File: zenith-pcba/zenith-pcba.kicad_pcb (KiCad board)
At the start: 2 copper layers, 45 parts, among them SW1 G4R152312, U1 XC7K70T-FBG676, U2 K4B4G1646E-BCNB, U3 CH347T, U4 AP63203WU, U5 TXS0101DB, U6 TXS0101DB, U7 TXS0101DB, U8 TXS0101DB, X1 SX5B8.000F1520F30

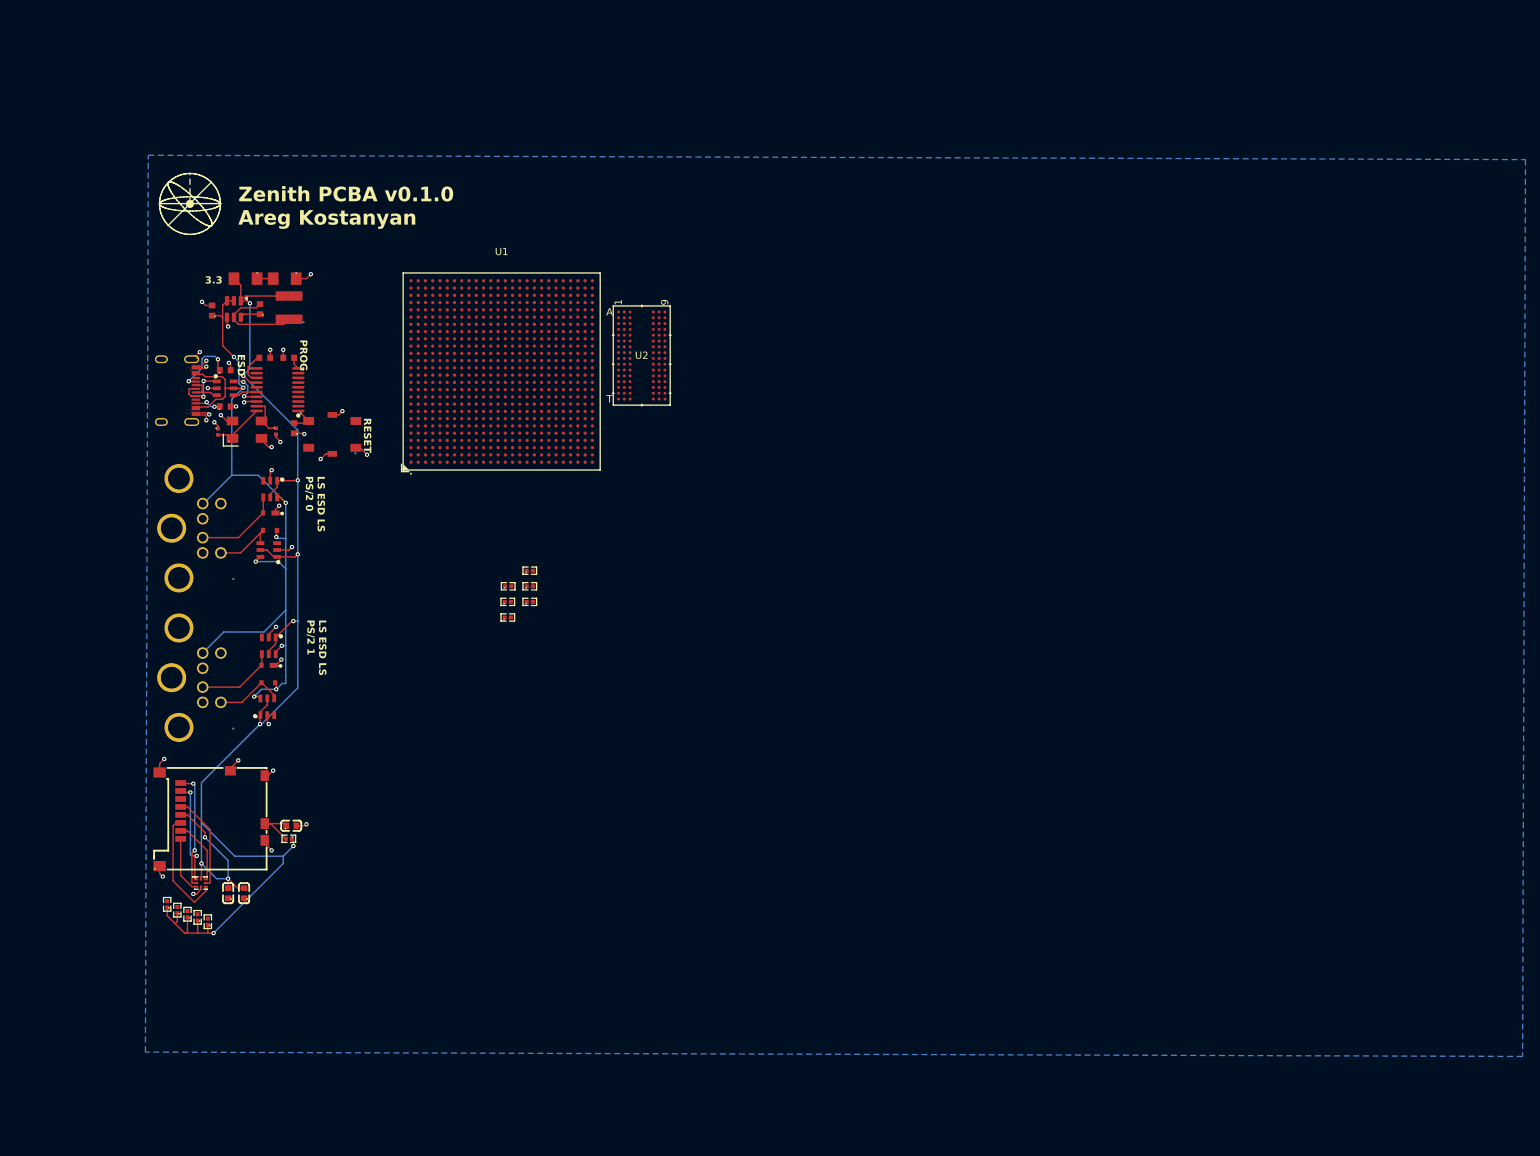
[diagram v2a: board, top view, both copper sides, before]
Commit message: feat(pcba): pcb edge cuts
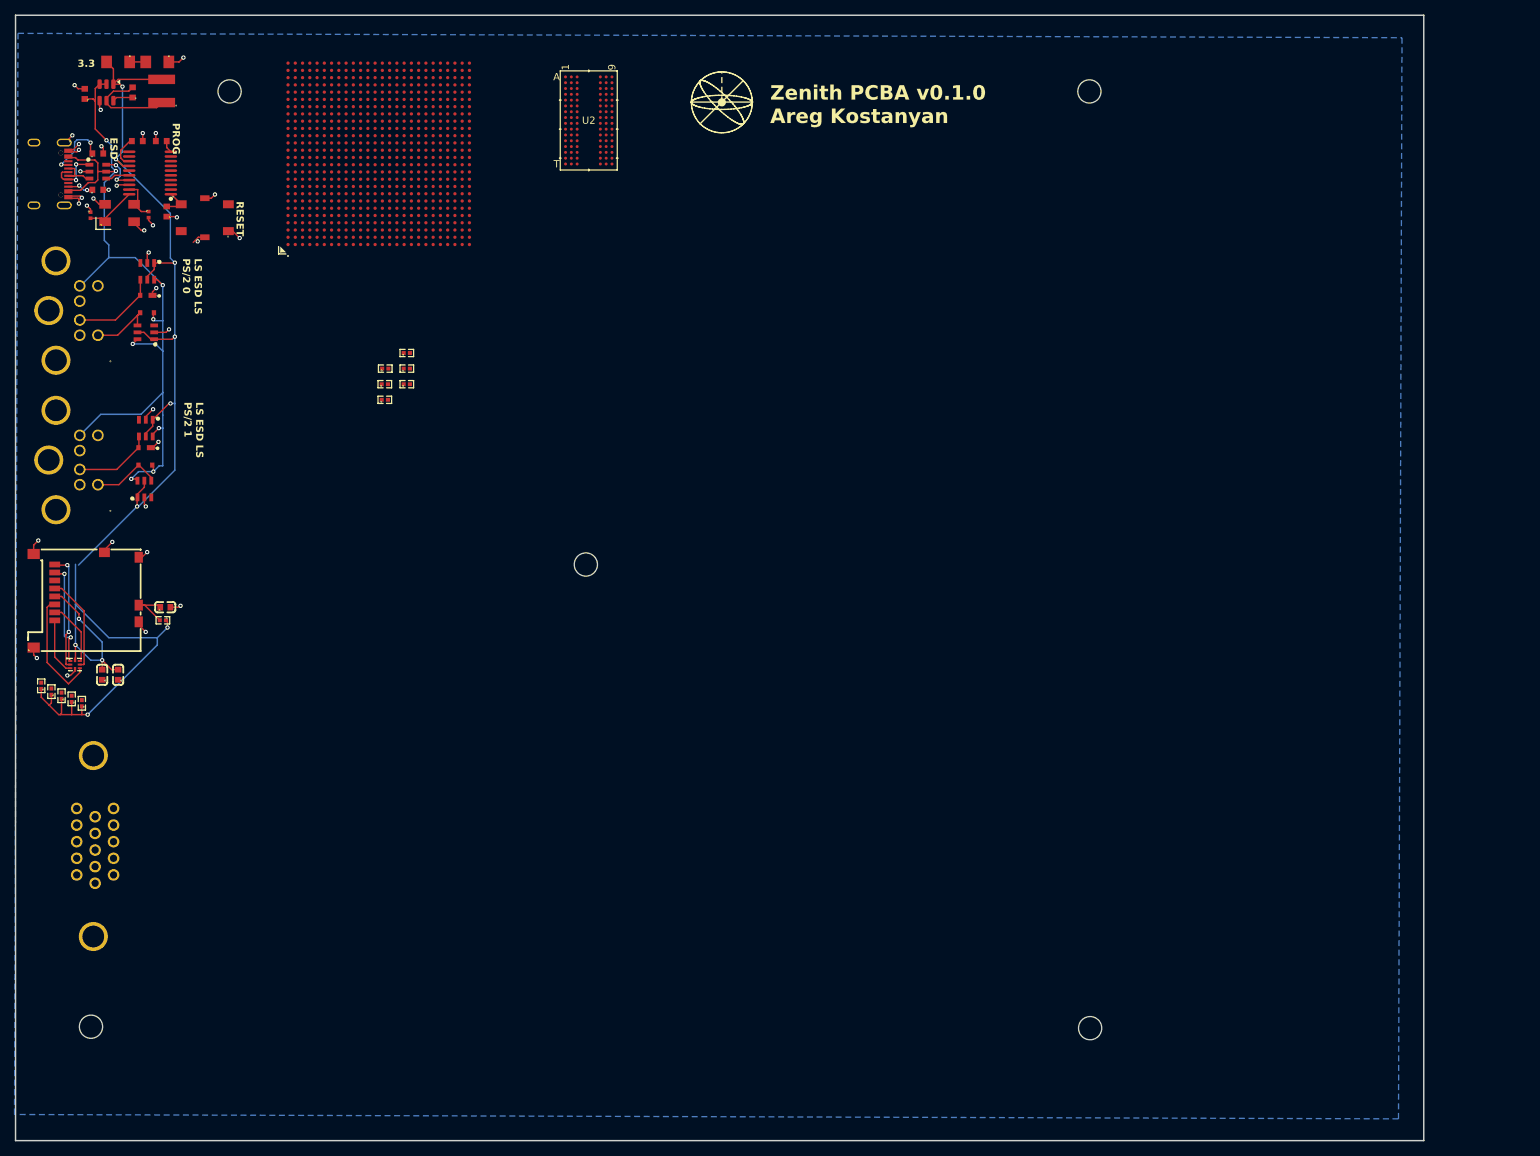
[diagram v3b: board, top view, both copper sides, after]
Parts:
- added DSub1: DS1038-15FBNSIA74-0CC, easyeda2kicad:DSUB-TH_DS1038-15FBNSIA74-0CC, F.Cu at (50.1, 129.2)
- added REF**: MountingHole_3.2mm_M3, MountingHole:MountingHole_3.2mm_M3, F.Cu at (117.7, 90.4)
- added REF**: MountingHole_3.2mm_M3, MountingHole:MountingHole_3.2mm_M3, F.Cu at (49.5, 154.1)
- added REF**: MountingHole_3.2mm_M3, MountingHole:MountingHole_3.2mm_M3, F.Cu at (187.2, 154.3)
- added REF**: MountingHole_3.2mm_M3, MountingHole:MountingHole_3.2mm_M3, F.Cu at (68.6, 25.2)
- added REF**: MountingHole_3.2mm_M3, MountingHole:MountingHole_3.2mm_M3, F.Cu at (187.1, 25.2)
- moved D4 34.8 mm to (47.3, 104.2)
- moved C8 34.8 mm to (59.7, 96.3)
- moved Card1 34.8 mm to (48.8, 95.3)
- moved R5 34.8 mm to (45.4, 108.5)
- moved R6 34.8 mm to (46.8, 108.9)
- moved R7 34.8 mm to (48.2, 109.5)
- moved R9 34.8 mm to (44.0, 107.9)
- moved C9 34.8 mm to (51.0, 105.6)
- moved R16 34.8 mm to (59.4, 98.1)
- moved R8 34.8 mm to (42.6, 107.1)
- moved C10 34.8 mm to (53.2, 105.6)
- moved C6 34.6 mm to (53.2, 21.1)
- moved C7 34.6 mm to (58.6, 21.1)
- moved L2 34.6 mm to (59.2, 25.1)
- moved C1 34.6 mm to (59.9, 41.8)
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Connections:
- U1 pad AA8: unconnected-(U1D-IO_L8P_T1_33-PadAA8) -> /IO/VSYNC
- U1 pad AF7: unconnected-(U1D-IO_L7N_T1_33-PadAF7) -> /IO/HSYNC
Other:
- board outline added: 194.1 x 155.1 mm

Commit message: feat(pcba): vga
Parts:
- added R17: RC0402JR-07510RL, easyeda2kicad:R0402, F.Cu at (57.4, 133.8)
- added R18: RC0402FR-071K02L, easyeda2kicad:R0402, F.Cu at (57.4, 132.0)
- added R19: RC0402JR-07510RL, easyeda2kicad:R0402, F.Cu at (57.4, 129.2)
- added R20: RC0402FR-071K02L, easyeda2kicad:R0402, F.Cu at (57.4, 125.6)
- added R21: RC0402JR-07510RL, easyeda2kicad:R0402, F.Cu at (57.4, 123.4)
- added R22: RC0402FR-071K02L, easyeda2kicad:R0402, F.Cu at (57.4, 121.6)
- added R23: RC0402DR-072K05L, easyeda2kicad:R0402, F.Cu at (57.4, 127.4)
- added REF**: MountingHole_3.2mm_M3, MountingHole:MountingHole_3.2mm_M3, F.Cu at (65.6, 63.8)
- added REF**: MountingHole_3.2mm_M3, MountingHole:MountingHole_3.2mm_M3, F.Cu at (57.8, 109.8)
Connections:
- net /IO/HSYNC renamed /IO/VGAHSYNC
- net /IO/VSYNC renamed /IO/VGAVSYNC
- DSub1 pad 1: unconnected-(DSub1-Pad1) -> Net-(DSub1-Pad1)
- DSub1 pad 2: unconnected-(DSub1-Pad2) -> Net-(DSub1-Pad2)
- DSub1 pad 3: unconnected-(DSub1-Pad3) -> Net-(DSub1-Pad3)
- U1 pad AA7: unconnected-(U1D-IO_L8N_T1_33-PadAA7) -> /IO/VGAR1
- U1 pad AA9: unconnected-(U1D-IO_L11P_T1_SRCC_33-PadAA9) -> /IO/VGAB1
- U1 pad AB7: unconnected-(U1D-IO_L10P_T1_33-PadAB7) -> /IO/VGAG1
- U1 pad AB9: unconnected-(U1D-IO_L11N_T1_SRCC_33-PadAB9) -> /IO/VGAB0
- U1 pad AC7: unconnected-(U1D-IO_L10N_T1_33-PadAC7) -> /IO/VGAG0
- U1 pad AC8: unconnected-(U1D-IO_L9P_T1_DQS_33-PadAC8) -> /IO/VGAR0
- U1 pad AD8: unconnected-(U1D-IO_L9N_T1_DQS_33-PadAD8) -> /IO/VGAG2
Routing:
- net GND: track 55.4 -> 106.9 mm, vias 35 -> 41
- net Net-(DSub1-Pad2): track 0.00 -> 12.9 mm
- net Net-(DSub1-Pad3): track 0.00 -> 11.0 mm
- net Net-(DSub1-Pad1): track 0.00 -> 6.03 mm
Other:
- board text added: "PROG RESET PROG ESD USB C"
- board text added: "SD ESD"
- board text added: "VGA"
- board text removed: "ESD"
- board text removed: "PROG"
- board text removed: "RESET"

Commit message: feat(pcba): vga level shifter
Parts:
- added D5: TPESD7538P, easyeda2kicad:DFN3810-9_L3.8-W1.0-P0.9, F.Cu at (59.0, 129.4)
- added U10: TXS0101DB, easyeda2kicad:SOT-23-6_L2.9-W1.6-P0.95-LS2.9-BL, F.Cu at (64.0, 119.2)
- added U9: TXS0101DB, easyeda2kicad:SOT-23-6_L2.9-W1.6-P0.95-LS2.9-BL, F.Cu at (59.7, 119.3)
- moved REF** 14.8 mm to (177.3, 143.3)
- moved R20 7.93 mm to (63.5, 130.6)
- moved R22 7.73 mm to (63.6, 126.2)
- moved R23 7.64 mm to (63.5, 132.0)
- moved R21 7.45 mm to (63.5, 127.6)
- moved R19 7.43 mm to (63.5, 133.4)
- moved R18 4.55 mm to (60.7, 135.2)
- moved R17 4.33 mm to (60.7, 136.6)
- moved REF** 3.31 mm to (49.3, 150.8)
- moved REF** 0.79 mm to (57.1, 109.3)
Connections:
- net Net-(DSub1-Pad1) renamed /IO/VGAR
- net Net-(DSub1-Pad2) renamed /IO/VGAG
- net Net-(DSub1-Pad3) renamed /IO/VGAB
- DSub1 pad 12: unconnected-(DSub1-Pad12) -> /IO/VGASDA5
- DSub1 pad 15: unconnected-(DSub1-Pad15) -> /IO/VGASCL5
- DSub1 pad 9: unconnected-(DSub1-Pad9) -> VCC5.0
- U1 pad AC9: unconnected-(U1D-IO_L12P_T1_MRCC_33-PadAC9) -> /IO/VGASDA
- U1 pad AD9: unconnected-(U1D-IO_L12N_T1_MRCC_33-PadAD9) -> /IO/VGASCL
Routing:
- net VCC5.0: track 114.4 -> 187.6 mm, vias 8 -> 13
- net GND: track 106.9 -> 65.2 mm, vias 41 -> 39
- net /IO/VGASCL5: track 0.00 -> 35.7 mm, vias 0 -> 2
- net /IO/VGASDA5: track 0.00 -> 31.8 mm, vias 0 -> 2
- net /IO/VGAHSYNC: track 0.00 -> 24.6 mm
- net VCC3.3: track 191.5 -> 215.6 mm
- net /IO/VGAVSYNC: track 0.00 -> 20.0 mm
- net /IO/VGAG: track 12.9 -> 26.4 mm, vias 0 -> 2
- net /IO/VGAR: track 6.03 -> 16.4 mm, vias 0 -> 4
- net /IO/VGAB: track 11.0 -> 18.1 mm, vias 0 -> 2
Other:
- board size 194.1 x 155.1 mm -> 194.1 x 141.7 mm
- board text added: "LS DAC ESD VGA"
- board text removed: "VGA"

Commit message: chore(pcba): clean up pages
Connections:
- U1 pad A1: unconnected-(U1H-GND-PadA1) -> GND
- U1 pad A16: unconnected-(U1H-GND-PadA16) -> GND
- U1 pad A2: unconnected-(U1H-GND-PadA2) -> GND
- U1 pad A26: unconnected-(U1H-GND-PadA26) -> GND
- U1 pad A5: unconnected-(U1H-GND-PadA5) -> GND
- U1 pad A6: unconnected-(U1H-GND-PadA6) -> GND
- U1 pad A7: unconnected-(U1H-GND-PadA7) -> GND
- U1 pad AA16: unconnected-(U1H-GND-PadAA16) -> GND
- U1 pad AA26: unconnected-(U1H-GND-PadAA26) -> GND
- U1 pad AA6: unconnected-(U1H-GND-PadAA6) -> GND
- U1 pad AB13: unconnected-(U1H-GND-PadAB13) -> GND
- U1 pad AB23: unconnected-(U1H-GND-PadAB23) -> GND
- U1 pad AB3: unconnected-(U1H-GND-PadAB3) -> GND
- U1 pad AC10: unconnected-(U1H-GND-PadAC10) -> GND
- U1 pad AC20: unconnected-(U1H-GND-PadAC20) -> GND
- U1 pad AD17: unconnected-(U1H-GND-PadAD17) -> GND
- U1 pad AD7: unconnected-(U1H-GND-PadAD7) -> GND
- U1 pad AE14: unconnected-(U1H-GND-PadAE14) -> GND
- U1 pad AE24: unconnected-(U1H-GND-PadAE24) -> GND
- U1 pad AE4: unconnected-(U1H-GND-PadAE4) -> GND
- U1 pad AF1: unconnected-(U1H-GND-PadAF1) -> GND
- U1 pad AF11: unconnected-(U1H-GND-PadAF11) -> GND
- U1 pad AF21: unconnected-(U1H-GND-PadAF21) -> GND
- U1 pad B13: unconnected-(U1H-GND-PadB13) -> GND
- U1 pad B23: unconnected-(U1H-GND-PadB23) -> GND
- U1 pad B4: unconnected-(U1H-GND-PadB4) -> GND
- U1 pad B7: unconnected-(U1H-GND-PadB7) -> GND
- U1 pad C1: unconnected-(U1H-GND-PadC1) -> GND
- U1 pad C10: unconnected-(U1H-GND-PadC10) -> GND
- U1 pad C20: unconnected-(U1H-GND-PadC20) -> GND
- U1 pad C5: unconnected-(U1H-GND-PadC5) -> GND
- U1 pad C7: unconnected-(U1H-GND-PadC7) -> GND
- U1 pad D17: unconnected-(U1H-GND-PadD17) -> GND
- U1 pad D4: unconnected-(U1H-GND-PadD4) -> GND
- U1 pad D7: unconnected-(U1H-GND-PadD7) -> GND
- U1 pad E1: unconnected-(U1H-GND-PadE1) -> GND
- U1 pad E14: unconnected-(U1H-GND-PadE14) -> GND
- U1 pad E2: unconnected-(U1H-GND-PadE2) -> GND
- U1 pad E24: unconnected-(U1H-GND-PadE24) -> GND
- U1 pad E5: unconnected-(U1H-GND-PadE5) -> GND
- U1 pad E7: unconnected-(U1H-GND-PadE7) -> GND
- U1 pad E8: unconnected-(U1H-VCCBATT_0-PadE8) -> VCC1.8
- U1 pad F11: unconnected-(U1H-GND-PadF11) -> GND
- U1 pad F21: unconnected-(U1H-GND-PadF21) -> GND
- U1 pad F3: unconnected-(U1H-GND-PadF3) -> GND
- U1 pad F4: unconnected-(U1H-GND-PadF4) -> GND
- U1 pad F7: unconnected-(U1H-GND-PadF7) -> GND
- U1 pad G1: unconnected-(U1H-GND-PadG1) -> GND
- U1 pad G18: unconnected-(U1H-GND-PadG18) -> GND
- U1 pad G5: unconnected-(U1H-GND-PadG5) -> GND
- U1 pad G8: unconnected-(U1H-GND-PadG8) -> GND
- U1 pad H15: unconnected-(U1H-GND-PadH15) -> GND
- U1 pad H25: unconnected-(U1H-GND-PadH25) -> GND
- U1 pad H4: unconnected-(U1H-GND-PadH4) -> GND
- U1 pad H7: unconnected-(U1H-GND-PadH7) -> GND
- U1 pad J1: unconnected-(U1H-GND-PadJ1) -> GND
- U1 pad J12: unconnected-(U1H-GND-PadJ12) -> GND
- U1 pad J2: unconnected-(U1H-GND-PadJ2) -> GND
- U1 pad J22: unconnected-(U1H-GND-PadJ22) -> GND
- U1 pad J5: unconnected-(U1H-GND-PadJ5) -> GND
- U1 pad J9: unconnected-(U1H-VCCINT-PadJ9) -> VCC1.0
- U1 pad K10: unconnected-(U1H-VCCINT-PadK10) -> VCC1.0
- U1 pad K11: unconnected-(U1H-GND-PadK11) -> GND
- U1 pad K12: unconnected-(U1H-VCCINT-PadK12) -> VCC1.0
- U1 pad K13: unconnected-(U1H-GND-PadK13) -> GND
- U1 pad K14: unconnected-(U1H-VCCINT-PadK14) -> VCC1.0
- U1 pad K19: unconnected-(U1H-GND-PadK19) -> GND
- U1 pad K3: unconnected-(U1H-GND-PadK3) -> GND
- U1 pad K4: unconnected-(U1H-GND-PadK4) -> GND
- U1 pad K7: unconnected-(U1H-GND-PadK7) -> GND
- U1 pad K8: unconnected-(U1H-VCCINT-PadK8) -> VCC1.0
- U1 pad K9: unconnected-(U1H-GND-PadK9) -> GND
- U1 pad L1: unconnected-(U1H-GND-PadL1) -> GND
- U1 pad L10: unconnected-(U1H-GND-PadL10) -> GND
- U1 pad L11: unconnected-(U1H-VCCAUX-PadL11) -> VCC1.8
- U1 pad L12: unconnected-(U1H-GND-PadL12) -> GND
- U1 pad L13: unconnected-(U1H-VCCINT-PadL13) -> VCC1.0
- U1 pad L14: unconnected-(U1H-GND-PadL14) -> GND
- U1 pad L15: unconnected-(U1H-VCCINT-PadL15) -> VCC1.0
- U1 pad L16: unconnected-(U1H-GND-PadL16) -> GND
- U1 pad L26: unconnected-(U1H-GND-PadL26) -> GND
- U1 pad L5: unconnected-(U1H-GND-PadL5) -> GND
- U1 pad L9: unconnected-(U1H-VCCINT-PadL9) -> VCC1.0
- U1 pad M10: unconnected-(U1H-VCCAUX-PadM10) -> VCC1.8
- U1 pad M11: unconnected-(U1H-GNDADC_0-PadM11) -> GND
- U1 pad M12: unconnected-(U1H-VCCADC_0-PadM12) -> VCC1.8
- U1 pad M13: unconnected-(U1H-GND-PadM13) -> GND
- U1 pad M14: unconnected-(U1H-VCCINT-PadM14) -> VCC1.0
- U1 pad M15: unconnected-(U1H-GND-PadM15) -> GND
- U1 pad M23: unconnected-(U1H-GND-PadM23) -> GND
- U1 pad M4: unconnected-(U1H-GND-PadM4) -> GND
- U1 pad M7: unconnected-(U1H-GND-PadM7) -> GND
- U1 pad M8: unconnected-(U1H-VCCINT-PadM8) -> VCC1.0
- U1 pad M9: unconnected-(U1H-GND-PadM9) -> GND
- U1 pad N1: unconnected-(U1H-GND-PadN1) -> GND
- U1 pad N10: unconnected-(U1H-GND-PadN10) -> GND
- U1 pad N13: unconnected-(U1H-VCCBRAM-PadN13) -> VCC1.0
- U1 pad N14: unconnected-(U1H-GND-PadN14) -> GND
- U1 pad N15: unconnected-(U1H-VCCINT-PadN15) -> VCC1.0
- U1 pad N2: unconnected-(U1H-GND-PadN2) -> GND
- U1 pad N20: unconnected-(U1H-GND-PadN20) -> GND
- U1 pad N5: unconnected-(U1H-GND-PadN5) -> GND
- U1 pad N7: unconnected-(U1H-GND-PadN7) -> GND
- U1 pad N9: unconnected-(U1H-VCCINT-PadN9) -> VCC1.0
- U1 pad P10: unconnected-(U1H-VCCAUX-PadP10) -> VCC1.8
- U1 pad P13: unconnected-(U1H-GND-PadP13) -> GND
- U1 pad P14: unconnected-(U1H-VCCINT-PadP14) -> VCC1.0
- U1 pad P15: unconnected-(U1H-GND-PadP15) -> GND
- U1 pad P17: unconnected-(U1H-GND-PadP17) -> GND
- U1 pad P3: unconnected-(U1H-GND-PadP3) -> GND
- U1 pad P4: unconnected-(U1H-GND-PadP4) -> GND
- U1 pad P8: unconnected-(U1H-VCCAUX_IO_G0-PadP8) -> VCC1.8
- U1 pad P9: unconnected-(U1H-GND-PadP9) -> GND
- U1 pad R1: unconnected-(U1H-GND-PadR1) -> GND
- U1 pad R10: unconnected-(U1H-GND-PadR10) -> GND
- U1 pad R13: unconnected-(U1H-VCCBRAM-PadR13) -> VCC1.0
- U1 pad R14: unconnected-(U1H-GND-PadR14) -> GND
- U1 pad R15: unconnected-(U1H-VCCINT-PadR15) -> VCC1.0
- U1 pad R2: unconnected-(U1H-GND-PadR2) -> GND
- U1 pad R24: unconnected-(U1H-GND-PadR24) -> GND
- U1 pad R5: unconnected-(U1H-GND-PadR5) -> GND
- U1 pad R8: unconnected-(U1H-GND-PadR8) -> GND
- U1 pad R9: unconnected-(U1H-VCCAUX_IO_G0-PadR9) -> VCC1.8
- U1 pad T1: unconnected-(U1H-GND-PadT1) -> GND
- U1 pad T10: unconnected-(U1H-VCCAUX-PadT10) -> VCC1.8
- U1 pad T11: unconnected-(U1H-GND-PadT11) -> GND
- U1 pad T12: unconnected-(U1H-VCCBRAM-PadT12) -> VCC1.0
- U1 pad T13: unconnected-(U1H-GND-PadT13) -> GND
- U1 pad T14: unconnected-(U1H-VCCINT-PadT14) -> VCC1.0
- U1 pad T15: unconnected-(U1H-GND-PadT15) -> GND
- U1 pad T21: unconnected-(U1H-GND-PadT21) -> GND
- U1 pad T3: unconnected-(U1H-GND-PadT3) -> GND
- U1 pad T4: unconnected-(U1H-GND-PadT4) -> GND
- U1 pad T8: unconnected-(U1H-VCCAUX_IO_G0-PadT8) -> VCC1.8
- U1 pad T9: unconnected-(U1H-GND-PadT9) -> GND
- U1 pad U10: unconnected-(U1H-GND-PadU10) -> GND
- U1 pad U11: unconnected-(U1H-VCCAUX-PadU11) -> VCC1.8
- U1 pad U12: unconnected-(U1H-GND-PadU12) -> GND
- U1 pad U13: unconnected-(U1H-VCCBRAM-PadU13) -> VCC1.0
- U1 pad U14: unconnected-(U1H-GND-PadU14) -> GND
- U1 pad U15: unconnected-(U1H-VCCINT-PadU15) -> VCC1.0
- U1 pad U18: unconnected-(U1H-GND-PadU18) -> GND
- U1 pad U8: unconnected-(U1H-GND-PadU8) -> GND
- U1 pad V15: unconnected-(U1H-GND-PadV15) -> GND
- U1 pad V25: unconnected-(U1H-GND-PadV25) -> GND
- U1 pad V5: unconnected-(U1H-GND-PadV5) -> GND
- U1 pad W12: unconnected-(U1H-GND-PadW12) -> GND
- U1 pad W2: unconnected-(U1H-GND-PadW2) -> GND
- U1 pad W22: unconnected-(U1H-GND-PadW22) -> GND
- U1 pad Y19: unconnected-(U1H-GND-PadY19) -> GND
- U1 pad Y9: unconnected-(U1H-GND-PadY9) -> GND
